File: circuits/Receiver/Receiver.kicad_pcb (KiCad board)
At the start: 4 copper layers, 107.4 x 10 mm, 33 parts, among them J1 ORA. . .12V, J10 DI, J11 GND, J2 ORA___12V, J3 GRN. . .12V, J4 BLU___A, J5 BLU. . .B, J6 GRN___GND, J7 BRN. . .GND, J8 BRN___GND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

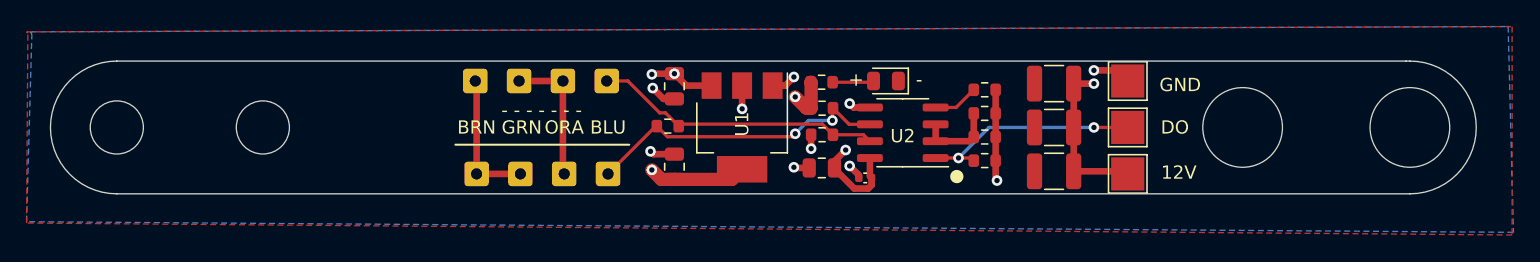
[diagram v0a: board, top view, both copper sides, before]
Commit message: Use zipties for strain relief on cables
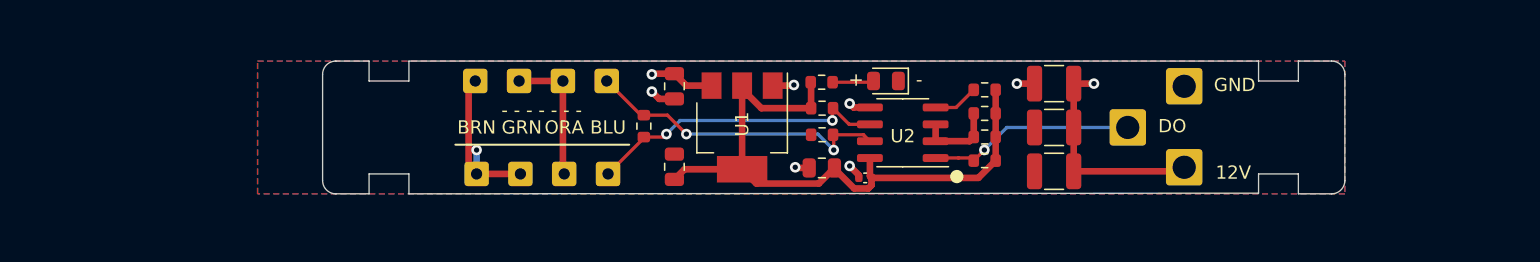
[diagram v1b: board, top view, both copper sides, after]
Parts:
- removed H1, H3: Strain Relief, MountingHole:MountingHole_4mm
- removed H2, H4: Strain Relief, MountingHole:MountingHole_6mm
- J10, J11, J9: footprint TestPoint:TestPoint_Pad_2.5x2.5mm -> Connector_Wire:SolderWire-1sqmm_1x01_D1.4mm_OD2.7mm
- moved J9 4.28 mm to (105.4, 77.0)
- moved J11 4.27 mm to (105.4, 70.9)
- moved R8 1.80 mm to (64.7, 73.9), turned to -90 degrees
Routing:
- net +5V: track 26.9 -> 48.5 mm, vias 5 -> 0
- net +12V: track 27.5 -> 31.8 mm, vias 3 -> 2
- net GND: track 30.1 -> 27.5 mm, vias 8 -> 7
- net /B: track 21.4 -> 23.4 mm, vias 0 -> 2
- net /LED DI: track 16.7 -> 15.6 mm, vias 2 -> 1
- net /A: track 23.5 -> 22.8 mm
- added copper zone on B.Cu, net +12V
- removed copper zone on B.Cu, net +5V
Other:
- board size 107.4 x 10 mm -> 77 x 10 mm

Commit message: 1.0 sent to production
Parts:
- added H1: JLCPCB Tooling, Joels KiCad Footprint Library:JCLPCB_Tooling_Hole, F.Cu at (43.5, 74.4)
- added H2: JLCPCB Tooling, Joels KiCad Footprint Library:JCLPCB_Tooling_Hole, F.Cu at (114.5, 74.1)
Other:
- board text added: "CAT-6 TO WS2815B WITH POWER JOEL SPOLSKY https://blinkylights.blog USE 23awg CABLE OR BETTER"
- board text added: "JLCJLCJLCJLC"
